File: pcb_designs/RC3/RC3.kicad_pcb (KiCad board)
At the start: 2 copper layers, 100 x 100 mm, 50 parts, among them J1 Conn_01x07_Socket, J10 Comms & ADC, J11 I2C OLED, J12 Conn_01x04_Pin, J2 Conn_01x07_Socket, J3 DCC Out, J4 DC In, J5 Barrel_Jack_Switch, J6 GPIO, J7 I2C Off Board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

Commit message: PCB RC3 Update
PCB RC3 Layout Updated
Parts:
- D5, D6: value WS2812B -> SK6812; footprint LED_SMD:LED_WS2812B_PLCC4_5.0x5.0mm_P3.2mm -> LED_SMD:LED_SK6812_PLCC4_5.0x5.0mm_P3.2mm
- J10: value Comms & ADC -> Comms/ADC
- J12: value Conn_01x04_Pin -> Test Points
- J3: value DCC Out -> TRACK
- J4: value DC In -> DC 12 - 16 V
- J7: value I2C Off Board -> I2C0
- JP1: value SolderJumper_2_Open -> Orientation
- moved J10 53.9 mm to (71.1, 30.5)
- moved C6 45.0 mm to (83.8, 48.3), turned to 90 degrees
- moved C7 35.4 mm to (78.7, 43.3), turned to -90 degrees
- moved U5 29.7 mm to (78.7, 30.5)
- moved R13 29.6 mm to (63.5, 61.0), turned to -90 degrees
- moved C8 27.2 mm to (83.8, 38.1)
- moved J6 25.0 mm to (33.0, 66.0)
- moved A1 23.4 mm to (40.6, 30.5)
- moved SW1 21.7 mm to (69.7, 53.9)
- moved J12 20.7 mm to (76.2, 85.1), turned to 0 degrees
- moved JP1 15.5 mm to (75.5, 76.2)
- moved D6 10.6 mm to (61.0, 96.8), turned to 180 degrees
- moved D5 10.6 mm to (50.8, 96.8), turned to 180 degrees
- moved J9 2.54 mm to (33.0, 38.1)
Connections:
- D5 pad 1: +5V -> GNDPWR
- D5 pad 2: Net-(D5-DOUT) -> Net-(D5-DIN)
- D5 pad 3: GNDPWR -> +5V
- D5 pad 4: Net-(D5-DIN) -> Net-(D5-DOUT)
- D6 pad 1: +5V -> GNDPWR
- D6 pad 2: Net-(D6-DOUT) -> Net-(D5-DOUT)
- D6 pad 3: GNDPWR -> +5V
- D6 pad 4: Net-(D5-DOUT) -> Net-(D6-DOUT)
- J10 pad 3: /GPIO17 -> /GPIO00
- J10 pad 4: /GPIO00 -> /GPIO01
- J10 pad 5: /GPIO01 -> /ADC2
- J10 pad 6: /ADC2 -> /AGND
- J10 pad 7: /AGND -> /ADC1
- J10 pad 8: /ADC1 -> /GPIO17
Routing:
- net /SPI1_MOSI: track 71.5 -> 18.4 mm
- net +3.3V: track 199.5 -> 246.6 mm, vias 1 -> 3
- net /SPI1_CS: track 50.7 -> 8.67 mm, vias 1 -> 0
- net /SPI1_MISO: track 48.6 -> 9.72 mm, vias 1 -> 0
- net /AGND: track 51.6 -> 14.8 mm, vias 2 -> 0
- net /ADC2: track 51.6 -> 14.8 mm, vias 2 -> 0
- net /ADC1: track 51.6 -> 14.8 mm, vias 2 -> 0
- net /GPIO15: track 39.3 -> 9.72 mm
- net /GPIO14: track 39.3 -> 9.72 mm
- net /SPI1_SCK: track 39.0 -> 9.72 mm, vias 1 -> 0
- net /DCC_CS: track 26.4 -> 55.3 mm, vias 0 -> 2
- net /NEO_P: track 33.2 -> 6.13 mm, vias 1 -> 0
- net +5V: track 131.6 -> 158.2 mm, vias 1 -> 0
- net /GPIO13: track 36.8 -> 10.8 mm
- net /GPIO12: track 36.8 -> 10.8 mm
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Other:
- board text added: "CmpH"
- board text added: "CmpL"
- board text removed: "Comms/ADC"
- board text removed: "DC 12 - 16 V"
- board text removed: "GPIO"
- board text removed: "I2C0"
- board text removed: "RESET"
- board text removed: "SPI1"
- board text removed: "TRACK"
- board text removed: "Test Points"

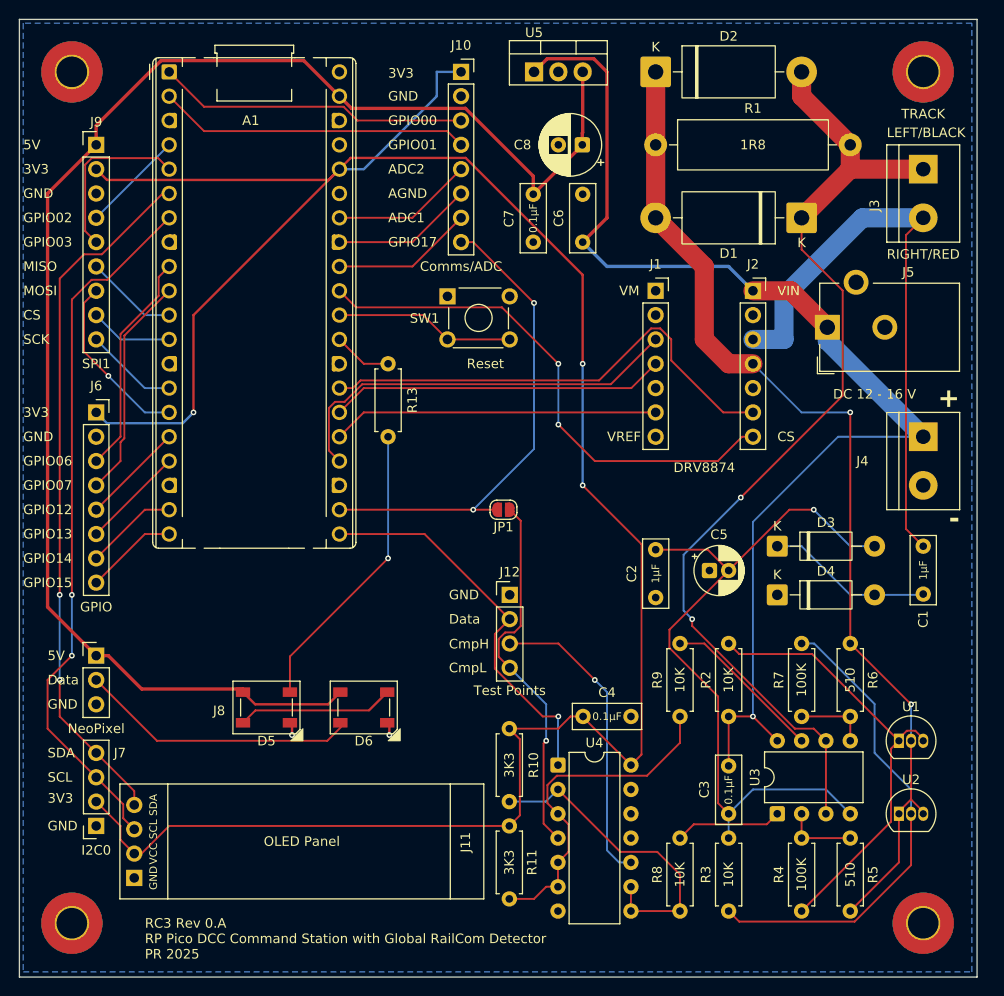
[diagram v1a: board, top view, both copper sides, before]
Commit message: MQTT Added & PCB RC3 Update
MQTT Client and associated modules added. RA3 PCB DRV8874 header corrected. Two main modules added; one for Command Station and Global RailCom Detector, one for Block/ local RailCom detector.
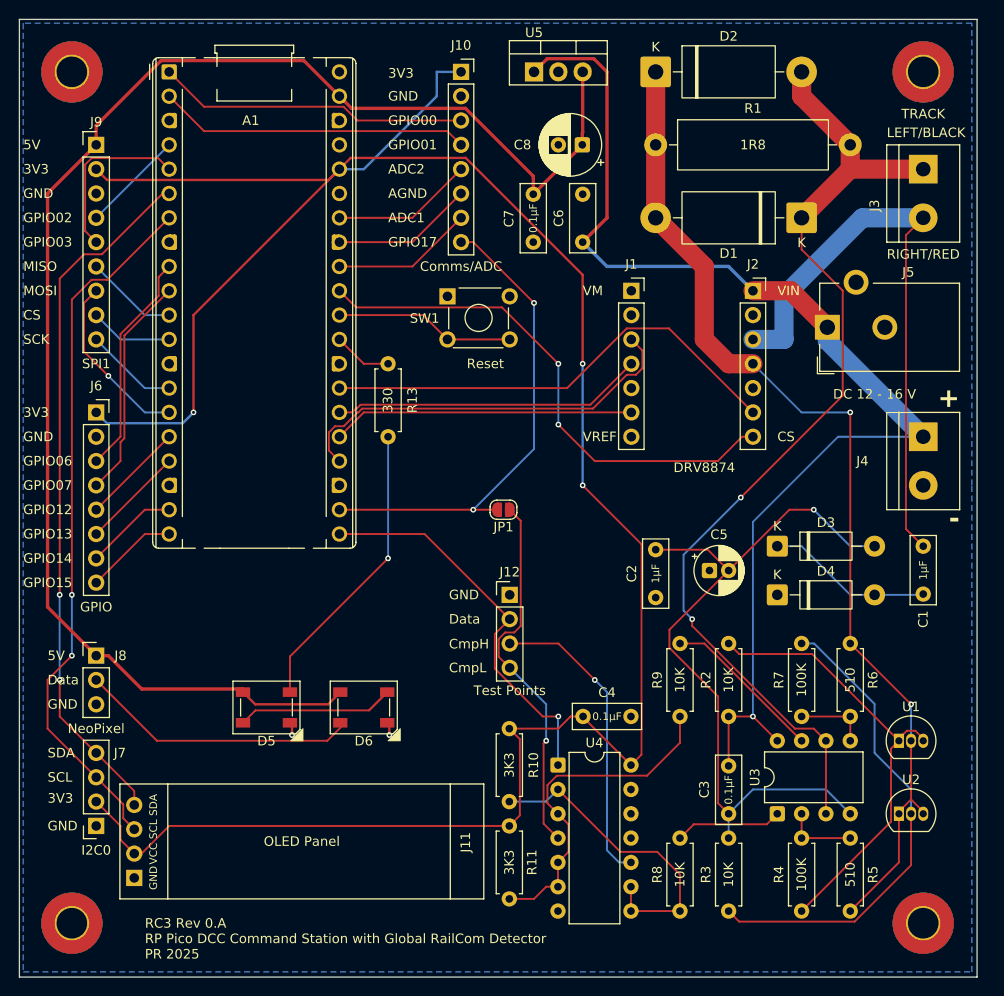
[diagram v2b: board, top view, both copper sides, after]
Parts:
- moved J1 2.54 mm to (88.9, 53.3)
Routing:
- net /DCC_PH: track 35.1 -> 32.6 mm
- net /~{DCC_SLEEP}: track 34.1 -> 31.5 mm
- net /~{DCC_FAULT}: track 50.7 -> 49.4 mm
- net /DCC_EN: track 43.1 -> 42.4 mm
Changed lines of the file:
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@@
 	(footprint "Connector_PinSocket_2.54mm:PinSocket_1x07_P2.54mm_Vertical"
 		(layer "F.Cu")
-		(at 91.44 53.34)
+		(at 88.9 53.34)
 		(descr "Through hole straight socket strip, 1x07, 2.54mm pitch, single row (from Kicad 4.0.7), script generated")
 		(tags "Through hole socket strip THT 1x07 2.54mm single row")
@@
 		(tags "Through hole pin header THT 1x03 2.54mm single row")
 		(property "Reference" "J8"
-			(at 12.831 5.749 0)
+			(at 2.54 0 0)
 			(layer "F.SilkS")
 			(effects
@@
 		)
 		(property "Value" "330"
-			(at 3.81 2.54 90)
-			(layer "F.Fab")
+			(at 3.81 0.02 90)
+			(layer "F.SilkS")
 			(effects
 				(font
@@
 	)
 	(gr_text "VREF"
-		(at 86.36 68.58 0)
+		(at 83.82 68.58 0)
 		(layer "F.SilkS")
 		(effects
@@
 	)
 	(gr_text "VM"
-		(at 87.63 53.34 0)
+		(at 83.82 53.34 0)
 		(layer "F.SilkS")
 		(effects
@@
 	)
 	(segment
-		(start 63.541 99.639)
-		(end 63.631 99.729)
-		(width 0.2)
-		(layer "F.Cu")
-		(net 3)
-	)
-	(segment
-		(start 53.381 99.639)
-		(end 53.471 99.729)
-		(width 0.2)
-		(layer "F.Cu")
-		(net 3)
-	)
-	(segment
 		(start 63.631 98.671)
 		(end 63.41 98.45)
@@
 	)
 	(segment
-		(start 57.319 70.019)
-		(end 57.319 65.58395)
+		(start 58.42 71.12)
+		(end 57.319 70.019)
 		(width 0.2)
 		(layer "F.Cu")
@@
 	)
 	(segment
-		(start 60.7939 63.099)
-		(end 86.761 63.099)
+		(start 60.31505 66.04)
+		(end 60.3929 66.04)
 		(width 0.2)
 		(layer "F.Cu")
@@
 	)
 	(segment
-		(start 57.96395 64.939)
-		(end 58.9539 64.939)
+		(start 58.87605 67.479)
+		(end 60.31505 66.04)
 		(width 0.2)
 		(layer "F.Cu")
@@
 	)
 	(segment
-		(start 86.761 63.099)
-		(end 91.44 58.42)
+		(start 60.3929 66.04)
+		(end 60.7939 65.639)
 		(width 0.2)
 		(layer "F.Cu")
@@
 	)
 	(segment
-		(start 57.319 65.58395)
-		(end 57.96395 64.939)
+		(start 90.051 61.43676)
+		(end 90.051 59.571)
 		(width 0.2)
 		(layer "F.Cu")
@@
 	)
 	(segment
-		(start 58.42 71.12)
-		(end 57.319 70.019)
+		(start 57.96395 67.479)
+		(end 58.87605 67.479)
+		(width 0.2)
+		(layer "F.Cu")
+		(net 7)
+	)
+	(segment
+		(start 90.051 59.571)
+		(end 88.9 58.42)
 		(width 0.2)
 		(layer "F.Cu")
@@
 	)
 	(segment
-		(start 58.9539 64.939)
-		(end 60.7939 63.099)
+		(start 57.319 70.019)
+		(end 57.319 68.12395)
+		(width 0.2)
+		(layer "F.Cu")
+		(net 7)
+	)
+	(segment
+		(start 84.89524 65.639)
+		(end 88.42324 62.111)
+		(width 0.2)
+		(layer "F.Cu")
+		(net 7)
+	)
+	(segment
+		(start 60.7939 65.639)
+		(end 84.89524 65.639)
+		(width 0.2)
+		(layer "F.Cu")
+		(net 7)
+	)
+	(segment
+		(start 57.319 68.12395)
+		(end 57.96395 67.479)
+		(width 0.2)
+		(layer "F.Cu")
+		(net 7)
+	)
+	(segment
+		(start 88.42324 62.111)
+		(end 89.37676 62.111)
+		(width 0.2)
+		(layer "F.Cu")
+		(net 7)
+	)
+	(segment
+		(start 89.37676 62.111)
+		(end 90.051 61.43676)
 		(width 0.2)
 		(layer "F.Cu")
@@
 	)
 	(segment
-		(start 88.9 63.5)
-		(end 91.44 60.96)
+		(start 60.14895 65.639)
+		(end 60.2268 65.639)
+		(width 0.2)
+		(layer "F.Cu")
+		(net 17)
+	)
+	(segment
+		(start 84.622 65.238)
+		(end 88.9 60.96)
 		(width 0.2)
 		(layer "F.Cu")
@@
 	)
 	(segment
-		(start 60.96 63.5)
-		(end 88.9 63.5)
+		(start 59.74795 66.04)
+		(end 60.14895 65.639)
+		(width 0.2)
+		(layer "F.Cu")
+		(net 17)
+	)
+	(segment
+		(start 60.2268 65.639)
+		(end 60.6278 65.238)
+		(width 0.2)
+		(layer "F.Cu")
+		(net 17)
+	)
+	(segment
+		(start 60.6278 65.238)
+		(end 84.622 65.238)
 		(width 0.2)
 		(layer "F.Cu")
@@
 	(segment
 		(start 58.42 66.04)
-		(end 60.96 63.5)
+		(end 59.74795 66.04)
 		(width 0.2)
 		(layer "F.Cu")
@@
 	)
 	(segment
-		(start 60.96 66.04)
-		(end 91.44 66.04)
+		(start 58.42 68.58)
+		(end 60.96 66.04)
 		(width 0.2)
 		(layer "F.Cu")
@@
 	)
 	(segment
-		(start 58.42 68.58)
-		(end 60.96 66.04)
+		(start 60.96 66.04)
+		(end 88.9 66.04)
 		(width 0.2)
 		(layer "F.Cu")
@@
 	)
 	(segment
-		(start 85.53424 62.698)
-		(end 90.96324 57.269)
-		(width 0.2)
-		(layer "F.Cu")
-		(net 32)
-	)
-	(segment
 		(start 58.42 63.5)
-		(end 59.8258 63.5)
+		(end 82.19224 63.5)
 		(width 0.2)
 		(layer "F.Cu")
@@
 	)
 	(segment
-		(start 91.91676 57.269)
-		(end 93.06776 58.42)
-		(width 0.2)
-		(layer "F.Cu")
-		(net 32)
-	)
-	(segment
-		(start 90.96324 57.269)
-		(end 91.91676 57.269)
-		(width 0.2)
-		(layer "F.Cu")
-		(net 32)
-	)
-	(segment
-		(start 98.4929 66.04)
+		(start 92.829 57.269)
 		(end 101.6 66.04)
 		(width 0.2)
@@
 	)
 	(segment
-		(start 93.06776 58.42)
-		(end 93.06776 60.61486)
-		(width 0.2)
-		(layer "F.Cu")
-		(net 32)
-	)
-	(segment
-		(start 93.06776 60.61486)
-		(end 98.4929 66.04)
-		(width 0.2)
-		(layer "F.Cu")
-		(net 32)
-	)
-	(segment
-		(start 59.8258 63.5)
-		(end 60.6278 62.698)
+		(start 88.42324 57.269)
+		(end 92.829 57.269)
 		(width 0.2)
 		(layer "F.Cu")
@@
 	)
 	(segment
-		(start 60.6278 62.698)
-		(end 85.53424 62.698)
+		(start 82.19224 63.5)
+		(end 88.42324 57.269)
 		(width 0.2)
 		(layer "F.Cu")
@@
 	)
 	(group ""
-		(members "5248e0b4-03e1-4b31-9a8e-f286c4c4c143" "9c524456-1387-4a67-ab1e-bec51be92fe2")
+		(members "e40e2045-3eab-4691-b4f3-c8d1f267d0aa")
 	)
 	(group ""
-		(members "e40e2045-3eab-4691-b4f3-c8d1f267d0aa")
+		(members "5248e0b4-03e1-4b31-9a8e-f286c4c4c143" "9c524456-1387-4a67-ab1e-bec51be92fe2")
 	)
 	(group ""
